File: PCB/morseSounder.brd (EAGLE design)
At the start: 56.6 x 82.7 mm, 75 parts, among them IC1 LM386M-1, IC5 LM321MF, J1 AVR_SPI_PRG_6PTH, J2 POWERPOLE_POWER25A_HORIZONTAL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, J3 POWER_JACKPTH, Q1 MMBT3904, Q2 MMBT3904, Q3 MMBT3904, T1 MMBTA42, U1 ATMEGA168

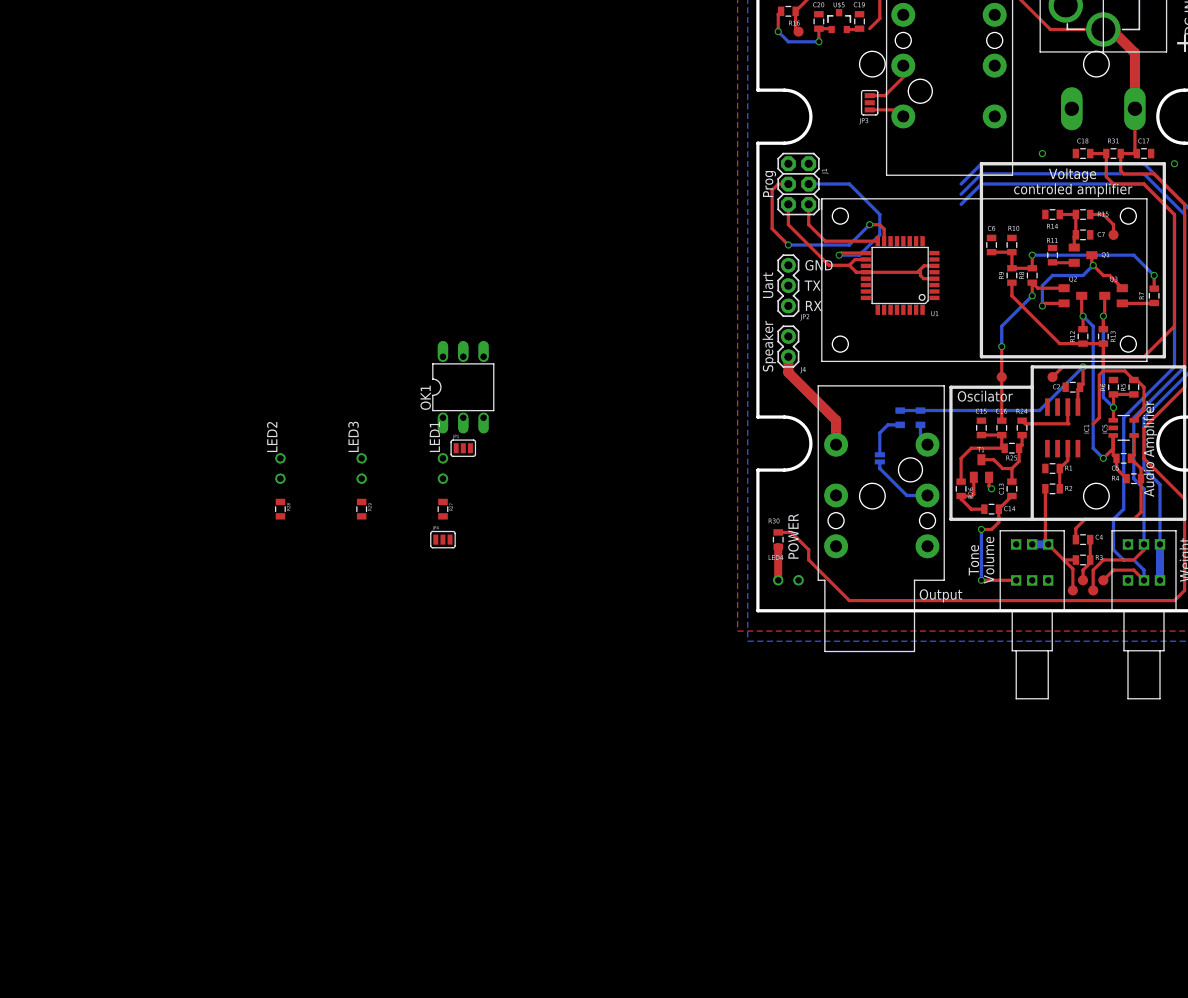
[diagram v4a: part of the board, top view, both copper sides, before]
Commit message: * Removed opto-isolator driving the amplifier. Swapped to a high side MOSFET driver.     Note this makes the micro mandatory. * Added input protection for the key.
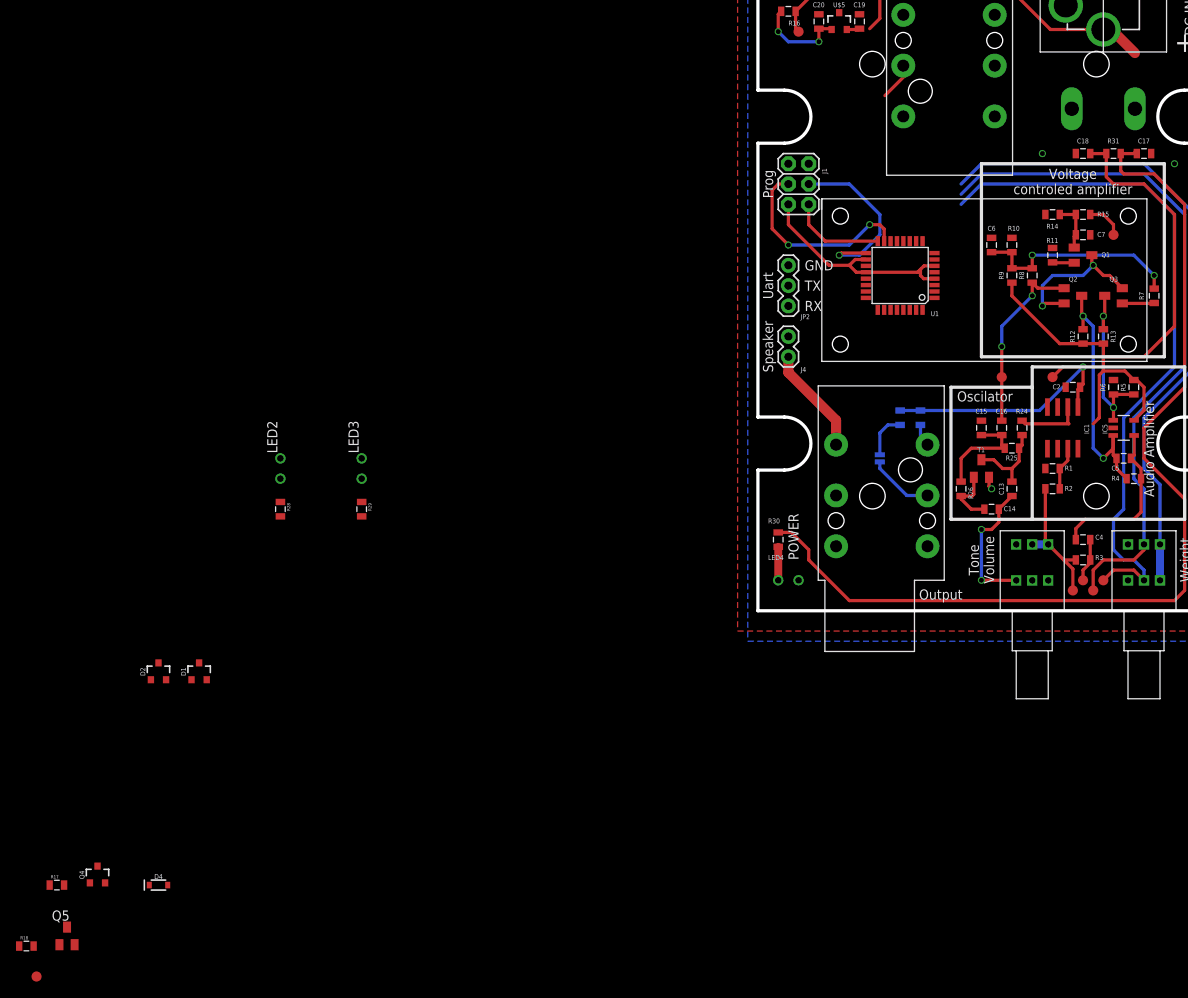
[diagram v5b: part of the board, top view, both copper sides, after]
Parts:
- removed JP1, JP3, JP4: JUMPER-3SMD, SparkFun:SJ_3
- removed LED1: (no value), SparkFun:LED3MM-NS
- removed OK1: 4N35, optocoupler:DIL06
- removed R27: 750, SparkFun:0805
- added D1, D2: 200mA/70V, SparkFun-DiscreteSemi:SOT23-3
- added D4: 0.5A/40V/420mV, SparkFun-DiscreteSemi:SOD-323
- added Q4: 2.5A/30V/105mΩ, SparkFun-DiscreteSemi:SOT23-3
- added Q5: MMBT3904, transistor:SOT23-BEC
- added R17, R18: 10k, SparkFun:0805
- added TP9: TEST-POINT3X5, SparkFun-Connectors:PAD.03X.05
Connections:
- removed net KEY_INPUT: JP1.1, JP3.2
- removed net N$10: LED1.K, OK1.1
- removed net N$30: JP4.2, R27.2
- removed net N$31: JP1.2, OK1.2
- removed net N$32: LED1.A, R27.1
- new net N$16: Q5.B, R18.2
- new net N$17: Q4.1, Q5.C, R17.1
- new net N$4: D4.A, J2.RED
- net +12V: now also Q4.2, R17.2; no longer JP4.3, OK1.5
- net AVR_KEY_OUT: now also R18.1, TP9.P$1; no longer JP4.1
- net AVR_VCC: now also D1.2, D2.2
- net GND: now also D1.1, D2.1, Q5.E; no longer JP1.3
- net KEY_DASH: now also D2.3; no longer JP3.3
- net KEY_DOT: now also D1.3; no longer JP3.1
- net KEY_IN: now also Q4.3; no longer OK1.4
- net VIN: now also D4.C; no longer J2.RED
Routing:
- net VIN: track 176.0 -> 163.7 mm
- net KEY_DOT: track 4.54 -> 1.16 mm
- net KEY_DASH: track 6.70 -> 4.80 mm

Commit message: * Oops! Power reverse protection diode should protect both power inputs!
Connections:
- net N$4: now also C17.2, D4.C, R30.2, R31.2; no longer D4.A, J2.RED
- net VIN: now also D4.A, J2.RED; no longer C17.2, D4.C, R30.2, R31.2
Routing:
- net N$4: track 0.00 -> 122.3 mm
- net VIN: track 163.7 -> 41.4 mm
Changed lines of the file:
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@@
 </signal>
 <signal name="VIN">
-<contactref element="R30" pad="2"/>
-<contactref element="R31" pad="2"/>
-<contactref element="C17" pad="2"/>
 <contactref element="J3" pad="PWR"/>
 <wire x1="43.18" y1="72.66" x2="44.18" y2="72.66" width="1.27" layer="1"/>
@@
 <wire x1="15.24" y1="77.486" x2="15.24" y2="74.03" width="0.4064" layer="1"/>
 <wire x1="13.97" y1="72.76" x2="15.24" y2="74.03" width="0.4064" layer="1"/>
-<wire x1="47.13" y1="57.38" x2="47.36" y2="57.15" width="0.4064" layer="1"/>
-<wire x1="47.36" y1="57.15" x2="45.35" y2="57.15" width="0.4064" layer="1"/>
-<wire x1="45.35" y1="57.15" x2="45.35" y2="54.98" width="0.4064" layer="1"/>
-<wire x1="45.35" y1="54.98" x2="45.72" y2="54.61" width="0.4064" layer="1"/>
-<wire x1="45.72" y1="54.61" x2="49.53" y2="54.61" width="0.4064" layer="1"/>
-<wire x1="49.53" y1="54.61" x2="53.34" y2="50.8" width="0.4064" layer="1"/>
-<wire x1="53.34" y1="50.8" x2="53.34" y2="27.94" width="0.4064" layer="1"/>
-<wire x1="53.34" y1="27.94" x2="48.26" y2="22.86" width="0.4064" layer="1"/>
-<wire x1="48.26" y1="22.86" x2="48.26" y2="19.05" width="0.4064" layer="1"/>
-<wire x1="48.26" y1="19.05" x2="53.34" y2="13.97" width="0.4064" layer="1"/>
-<wire x1="53.34" y1="13.97" x2="53.34" y2="2.54" width="0.4064" layer="1"/>
-<wire x1="53.34" y1="2.54" x2="52.07" y2="1.27" width="0.4064" layer="1"/>
-<wire x1="52.07" y1="1.27" x2="11.43" y2="1.27" width="0.4064" layer="1"/>
-<wire x1="11.43" y1="1.27" x2="6.35" y2="6.35" width="0.4064" layer="1"/>
-<wire x1="6.35" y1="6.35" x2="6.35" y2="7.62" width="0.4064" layer="1"/>
-<wire x1="6.35" y1="7.62" x2="4.18" y2="9.79" width="0.4064" layer="1"/>
-<wire x1="2.54" y1="9.79" x2="4.18" y2="9.79" width="0.4064" layer="1"/>
-<contactref element="D4" pad="C"/>
-<wire x1="2.54" y1="9.79" x2="-76.08" y2="-34.29" width="0" layer="19" extent="1-1"/>
-<wire x1="47.13" y1="69.71" x2="47.13" y2="57.38" width="0" layer="19" extent="1-1"/>
+<contactref element="D4" pad="A"/>
+<contactref element="J2" pad="RED"/>
+<wire x1="13.97" y1="72.76" x2="-73.78" y2="-34.29" width="0" layer="19" extent="1-1"/>
+<wire x1="47.13" y1="62.75" x2="47.13" y2="69.71" width="0" layer="19" extent="1-1"/>
 </signal>
 <signal name="N$36">
@@
 <wire x1="39.37" y1="5.22" x2="38.24" y2="6.35" width="0.4064" layer="1"/>
 </signal>
-<signal name="N$4">
-<contactref element="D4" pad="A"/>
-<contactref element="J2" pad="RED"/>
-<wire x1="47.13" y1="62.75" x2="-73.78" y2="-34.29" width="0" layer="19" extent="1-1"/>
-</signal>
 <signal name="N$17">
 <contactref element="Q4" pad="1"/>
@@
 <wire x1="-87.31" y1="-41.74" x2="-90.54" y2="-41.91" width="0" layer="19" extent="1-1"/>
 </signal>
+<signal name="N$4">
+<contactref element="R30" pad="2"/>
+<contactref element="R31" pad="2"/>
+<contactref element="C17" pad="2"/>
+<wire x1="47.13" y1="57.38" x2="47.36" y2="57.15" width="0.4064" layer="1"/>
+<wire x1="47.36" y1="57.15" x2="45.35" y2="57.15" width="0.4064" layer="1"/>
+<wire x1="45.35" y1="57.15" x2="45.35" y2="54.98" width="0.4064" layer="1"/>
+<wire x1="45.35" y1="54.98" x2="45.72" y2="54.61" width="0.4064" layer="1"/>
+<wire x1="45.72" y1="54.61" x2="49.53" y2="54.61" width="0.4064" layer="1"/>
+<wire x1="49.53" y1="54.61" x2="53.34" y2="50.8" width="0.4064" layer="1"/>
+<wire x1="53.34" y1="50.8" x2="53.34" y2="27.94" width="0.4064" layer="1"/>
+<wire x1="53.34" y1="27.94" x2="48.26" y2="22.86" width="0.4064" layer="1"/>
+<wire x1="48.26" y1="22.86" x2="48.26" y2="19.05" width="0.4064" layer="1"/>
+<wire x1="48.26" y1="19.05" x2="53.34" y2="13.97" width="0.4064" layer="1"/>
+<wire x1="53.34" y1="13.97" x2="53.34" y2="2.54" width="0.4064" layer="1"/>
+<wire x1="53.34" y1="2.54" x2="52.07" y2="1.27" width="0.4064" layer="1"/>
+<wire x1="52.07" y1="1.27" x2="11.43" y2="1.27" width="0.4064" layer="1"/>
+<wire x1="11.43" y1="1.27" x2="6.35" y2="6.35" width="0.4064" layer="1"/>
+<wire x1="6.35" y1="6.35" x2="6.35" y2="7.62" width="0.4064" layer="1"/>
+<wire x1="6.35" y1="7.62" x2="4.18" y2="9.79" width="0.4064" layer="1"/>
+<wire x1="2.54" y1="9.79" x2="4.18" y2="9.79" width="0.4064" layer="1"/>
+<contactref element="D4" pad="C"/>
+<wire x1="2.54" y1="9.79" x2="-76.08" y2="-34.29" width="0" layer="19" extent="1-1"/>
+</signal>
 </signals>

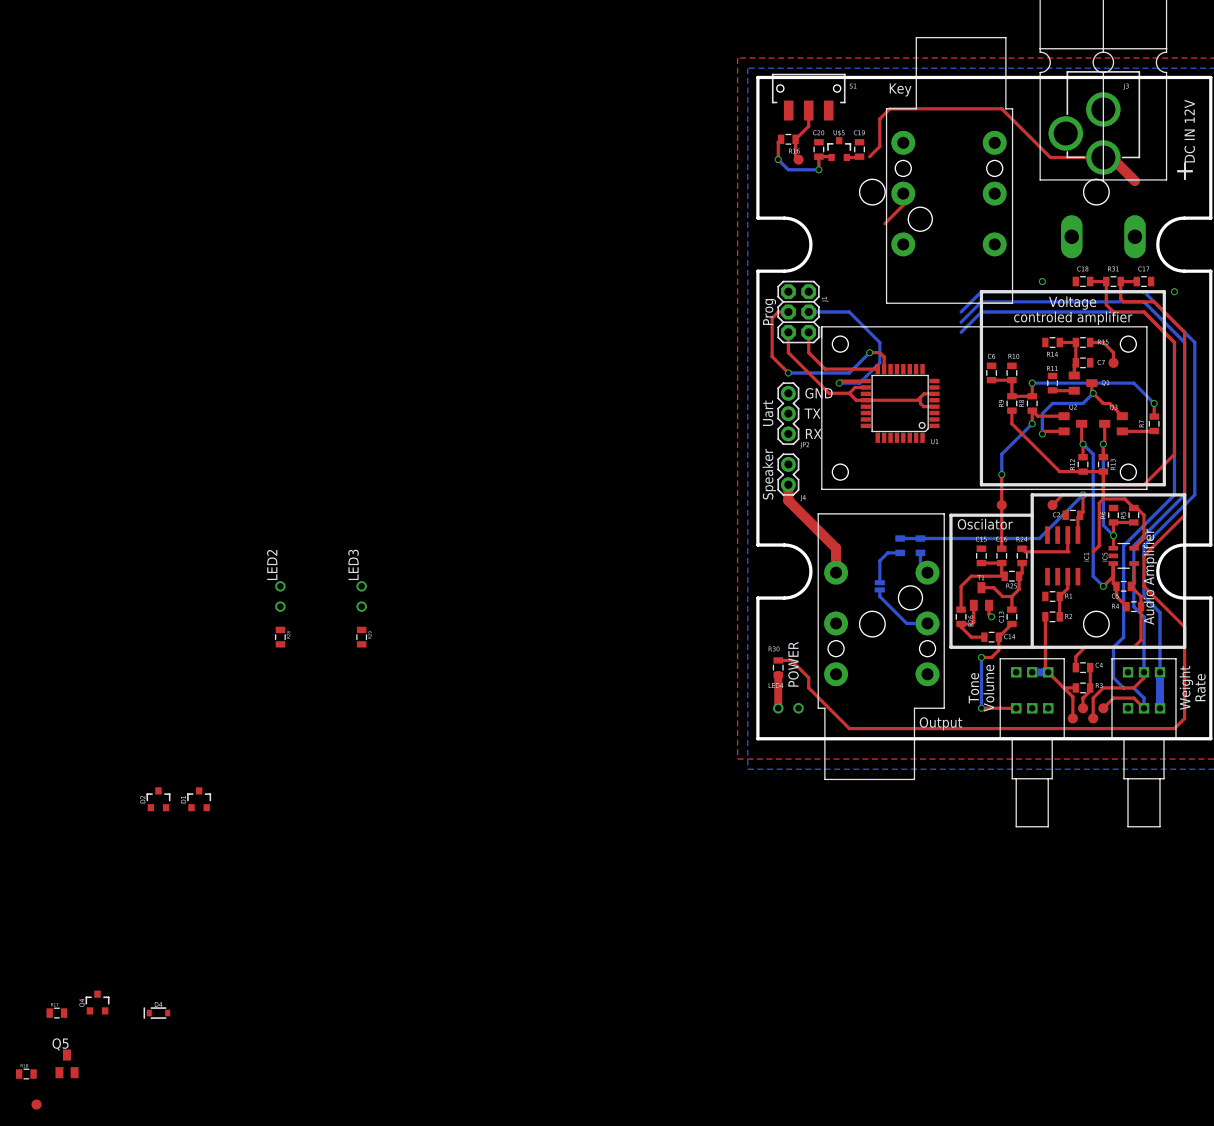
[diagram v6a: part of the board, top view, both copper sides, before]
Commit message: Routed rest of PCB
Altered pin placement on AVR
Added additional protection to key input
Separated LEDS from key input
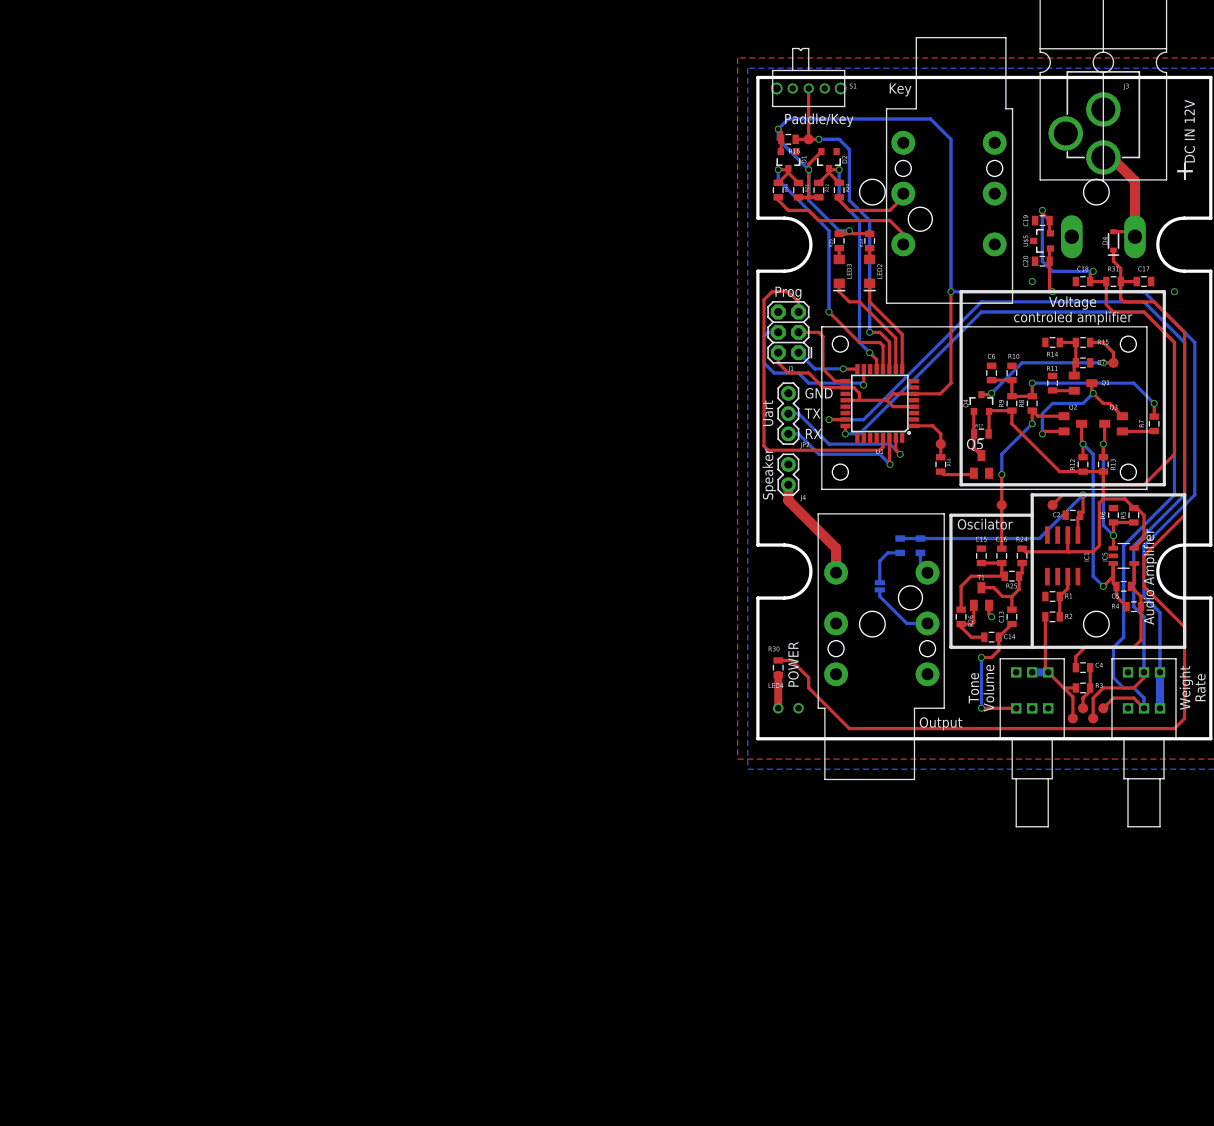
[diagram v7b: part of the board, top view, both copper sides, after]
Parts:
- added R19, R20: 470, SparkFun:0805
- added R21, R22: 15K, SparkFun:0805
- LED2, LED3: device SparkFun:LED3MM-NS -> SparkFun-LED:LED-1206
- S1: device SparkFun:SWITCH-SPDT-SMD -> morseSounder:TE-1825232-1
- U1: value ATMEGA168 -> ATMEGA328P_TQFP; device SparkFun:TQFP32-08 -> SparkFun-IC-Microcontroller:TQFP32-08
- moved D4 153.5 mm to (44.5, 62.2), turned to 90 degrees
- moved TP9 140.0 mm to (22.9, 36.8)
- moved R18 137.4 mm to (22.9, 34.3), turned to 270 degrees
- moved Q5 136.7 mm to (27.9, 34.3)
- moved R17 136.4 mm to (27.9, 38.1)
- moved Q4 133.5 mm to (27.9, 41.9)
- moved D2 115.9 mm to (8.89, 72.4), turned to 180 degrees
- moved D1 108.8 mm to (3.81, 72.4), turned to 180 degrees
- moved R28 88.8 mm to (14.0, 62.2), turned to 90 degrees
- moved LED2 84.1 mm to (14.0, 58.4), turned to 270 degrees
- moved R29 77.6 mm to (10.2, 62.2), turned to 90 degrees
- moved LED3 72.2 mm to (10.2, 58.4), turned to 270 degrees
- moved C20 31.2 mm to (35.6, 59.7), turned to 180 degrees
- moved U$5 27.9 mm to (35.6, 62.2), turned to 90 degrees
- moved C19 24.5 mm to (35.6, 64.8), turned to 180 degrees
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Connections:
- new net LED_DASH: LED3.C, U1.10
- new net LED_DOT: LED2.C, U1.9
- new net N$10: R20.2, U$1.P$5
- new net N$18: R19.2, U$1.P$6
- net AVR_KEY_MODE: now also U1.11; no longer U1.28
- net AVR_KEY_OUT: now also U1.1; no longer U1.27
- net AVR_VCC: now also R21.2, R22.2
- net KEY_DASH: now also R20.1, R22.1, U1.13; no longer LED3.K, U$1.P$5, U1.26
- net KEY_DOT: now also R19.1, R21.1, U1.12; no longer LED2.K, U$1.P$6, U1.25
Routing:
- net AVR_VCC: track 122.3 -> 208.7 mm, vias 2 -> 5
- net AVR_RESET: track 0.00 -> 41.2 mm
- net AVR_KEY_MODE: track 6.97 -> 43.9 mm, vias 0 -> 2
- net KEY_DOT: track 1.16 -> 37.3 mm, vias 0 -> 2
- net KEY_DASH: track 4.80 -> 32.3 mm, vias 0 -> 2
- net VIN: track 41.4 -> 15.1 mm
- net +12V: track 86.3 -> 111.3 mm, vias 0 -> 2
- net ADC_WEIGHT: track 86.1 -> 109.7 mm, vias 0 -> 1
- net ADC_RATE: track 86.7 -> 107.4 mm, vias 0 -> 1
- net N$18: track 0.00 -> 19.1 mm
- net AVR_TX: track 0.00 -> 18.4 mm, vias 0 -> 1
- net KEY_IN: track 4.71 -> 22.9 mm, vias 0 -> 2
- net AVR_RX: track 0.00 -> 17.6 mm, vias 0 -> 1
- net LED_DASH: track 0.00 -> 14.4 mm
- net LED_DOT: track 0.00 -> 12.4 mm
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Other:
- board text added: "Paddle/Key"
